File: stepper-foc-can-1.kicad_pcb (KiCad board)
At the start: 4 copper layers, 42 x 48 mm, 87 parts, among them J1 TC2030, J2 Conn_01x02, J3 Conn_01x04_Pin, J4 Conn_01x02, J5 Conn_01x02, M1 Stepper_Motor_bipolar, SW1 SW_Push, SW2 SW_Push, SW3 SW_Push, SW4 SW_Push, U1 STM32G474RBTx, U2 MX25947, U3 TPS62933, U4 TCAN3413, U5 AS5047P, U6 DRV8874, U7 INA241A3IDDF, U8 DRV8874, U9 INA241A3IDDF, Y1 Crystal_GND24

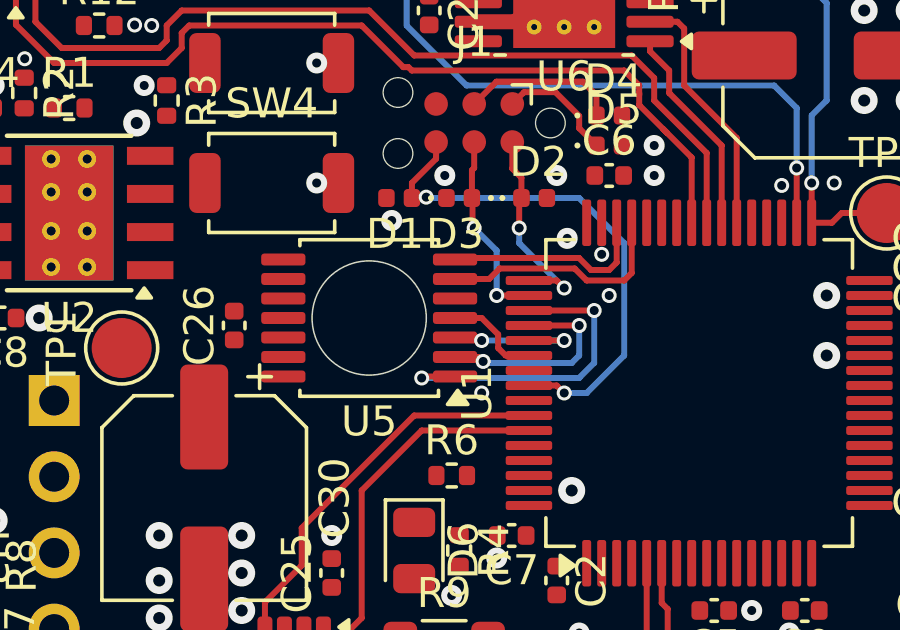
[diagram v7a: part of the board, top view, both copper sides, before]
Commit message: pcb: route encoder
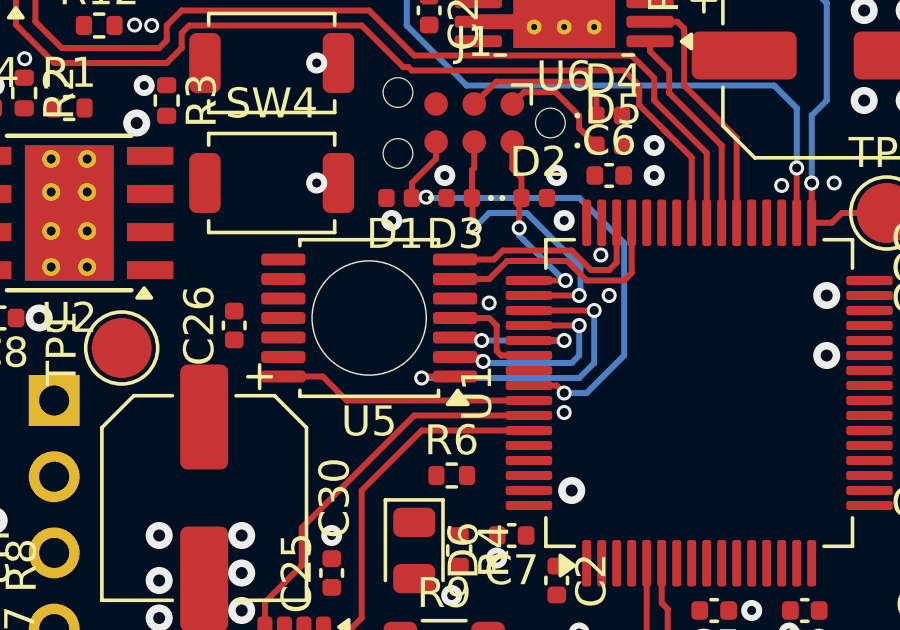
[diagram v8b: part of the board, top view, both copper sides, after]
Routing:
- net /ENC_I: track 0.00 -> 8.52 mm
- net /SWCLK: track 6.55 -> 10.1 mm
- net GND: vias 87 -> 88
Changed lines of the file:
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@@
 	)
 	(via
-		(at 150.6 78.346125)
+		(at 148 80.5)
+		(size 0.5)
+		(drill 0.3)
+		(layers "F.Cu" "B.Cu")
+		(net "GND")
+	)
+	(via
+		(at 150.5 77.75)
 		(size 0.7)
 		(drill 0.3)
@@
 	)
 	(via
-		(at 151.75 78.877587)
+		(at 151.721446 78.9)
 		(size 0.5)
 		(drill 0.3)
@@
 	)
 	(via
-		(at 147.75 83.5)
+		(at 150.5 84.150003)
 		(size 0.5)
 		(drill 0.3)
@@
 	)
 	(segment
-		(start 147.75 81)
-		(end 148.3 81.55)
+		(start 148.25 82.1)
+		(end 148.4 82.25)
 		(width 0.2)
 		(layer "F.Cu")
@@
 	(segment
 		(start 146.8625 81)
-		(end 147.75 81)
+		(end 148 81)
 		(width 0.2)
 		(layer "F.Cu")
@@
 	)
 	(segment
-		(start 148.3 81.999999)
-		(end 148.550001 82.25)
+		(start 148.25 81.25)
+		(end 148.25 82.1)
 		(width 0.2)
 		(layer "F.Cu")
@@
 	)
 	(segment
-		(start 148.550001 82.25)
+		(start 148 81)
+		(end 148.25 81.25)
+		(width 0.2)
+		(layer "F.Cu")
+		(net "/SPI_MOSI")
+	)
+	(segment
+		(start 148.4 82.25)
 		(end 149.325 82.25)
 		(width 0.2)
@@
 	)
 	(segment
-		(start 148.3 81.55)
-		(end 148.3 81.999999)
-		(width 0.2)
-		(layer "F.Cu")
-		(net "/SPI_MOSI")
+		(start 151.25 79.75)
+		(end 152.5 79.75)
+		(width 0.2)
+		(layer "F.Cu")
+		(net "/ENC_B")
+	)
+	(segment
+		(start 148.6 79.1)
+		(end 150.6 79.1)
+		(width 0.2)
+		(layer "F.Cu")
+		(net "/ENC_B")
+	)
+	(segment
+		(start 146.8625 79.7)
+		(end 148 79.7)
+		(width 0.2)
+		(layer "F.Cu")
+		(net "/ENC_B")
+	)
+	(segment
+		(start 152.5 79.75)
+		(end 152.75 79.5)
+		(width 0.2)
+		(layer "F.Cu")
+		(net "/ENC_B")
+	)
+	(segment
+		(start 148 79.7)
+		(end 148.6 79.1)
+		(width 0.2)
+		(layer "F.Cu")
+		(net "/ENC_B")
 	)
 	(segment
@@
 	)
 	(segment
-		(start 146.8625 79.7)
-		(end 148 79.7)
+		(start 150.6 79.1)
+		(end 151.25 79.75)
 		(width 0.2)
 		(layer "F.Cu")
@@
 	)
 	(segment
-		(start 150.85 79.35)
-		(end 151.25 79.75)
-		(width 0.2)
-		(layer "F.Cu")
-		(net "/ENC_B")
-	)
-	(segment
-		(start 151.25 79.75)
-		(end 152.5 79.75)
-		(width 0.2)
-		(layer "F.Cu")
-		(net "/ENC_B")
-	)
-	(segment
-		(start 148 79.7)
-		(end 148.35 79.35)
-		(width 0.2)
-		(layer "F.Cu")
-		(net "/ENC_B")
-	)
-	(segment
-		(start 148.35 79.35)
-		(end 150.85 79.35)
-		(width 0.2)
-		(layer "F.Cu")
-		(net "/ENC_B")
-	)
-	(segment
-		(start 152.5 79.75)
-		(end 152.75 79.5)
-		(width 0.2)
-		(layer "F.Cu")
-		(net "/ENC_B")
-	)
-	(segment
-		(start 150.994974 79)
-		(end 146.9125 79)
+		(start 148.455026 78.75)
+		(end 150.744974 78.75)
 		(width 0.2)
 		(layer "F.Cu")
@@
 	)
 	(segment
-		(start 152.25 77.825)
+		(start 146.8625 79.05)
+		(end 148.155026 79.05)
+		(width 0.2)
+		(layer "F.Cu")
+		(net "/ENC_A")
+	)
+	(segment
+		(start 148.155026 79.05)
+		(end 148.455026 78.75)
+		(width 0.2)
+		(layer "F.Cu")
+		(net "/ENC_A")
+	)
+	(segment
+		(start 152.25 79.15)
+		(end 152.25 77.825)
+		(width 0.2)
+		(layer "F.Cu")
+		(net "/ENC_A")
+	)
+	(segment
+		(start 150.744974 78.75)
+		(end 151.394974 79.4)
+		(width 0.2)
+		(layer "F.Cu")
+		(net "/ENC_A")
+	)
+	(segment
+		(start 151.394974 79.4)
+		(end 152 79.4)
+		(width 0.2)
+		(layer "F.Cu")
+		(net "/ENC_A")
+	)
+	(segment
+		(start 152 79.4)
 		(end 152.25 79.15)
-		(width 0.2)
-		(layer "F.Cu")
-		(net "/ENC_A")
-	)
-	(segment
-		(start 146.9125 79)
-		(end 146.8625 79.05)
-		(width 0.2)
-		(layer "F.Cu")
-		(net "/ENC_A")
-	)
-	(segment
-		(start 152.25 79.15)
-		(end 152 79.4)
-		(width 0.2)
-		(layer "F.Cu")
-		(net "/ENC_A")
-	)
-	(segment
-		(start 151.394974 79.4)
-		(end 150.994974 79)
-		(width 0.2)
-		(layer "F.Cu")
-		(net "/ENC_A")
-	)
-	(segment
-		(start 152 79.4)
-		(end 151.394974 79.4)
 		(width 0.2)
 		(layer "F.Cu")
@@
 	)
 	(segment
+		(start 143.25 83.75)
+		(end 142.45 82.95)
+		(width 0.2)
+		(layer "F.Cu")
+		(net "/ENC_I")
+	)
+	(segment
+		(start 149.325 83.75)
+		(end 143.25 83.75)
+		(width 0.2)
+		(layer "F.Cu")
+		(net "/ENC_I")
+	)
+	(segment
+		(start 142.45 82.95)
+		(end 141.1375 82.95)
+		(width 0.2)
+		(layer "F.Cu")
+		(net "/ENC_I")
+	)
+	(segment
 		(start 147.5 73.865)
 		(end 148.243699 73.121301)
@@
 	)
 	(segment
+		(start 150.542892 79.75)
+		(end 149.325 79.75)
+		(width 0.2)
+		(layer "F.Cu")
+		(net "/SWDIO")
+	)
+	(segment
 		(start 149 77.095)
 		(end 149.095 77)
@@
 	)
 	(segment
-		(start 150.25 79.75)
-		(end 150.5 80)
-		(width 0.2)
-		(layer "F.Cu")
-		(net "/SWDIO")
-	)
-	(segment
-		(start 149.325 79.75)
-		(end 150.25 79.75)
-		(width 0.2)
-		(layer "F.Cu")
-		(net "/SWDIO")
-	)
-	(segment
 		(start 149.075 76.325)
 		(end 149.075 77)
@@
 	)
 	(via
-		(at 150.5 80)
+		(at 150.542892 79.75)
 		(size 0.5)
 		(drill 0.3)
@@
 	)
 	(segment
-		(start 150.5 80)
-		(end 149 78.5)
+		(start 150.542892 79.75)
+		(end 150.5 79.75)
 		(width 0.2)
 		(layer "B.Cu")
@@
 	)
 	(segment
-		(start 149 78.5)
+		(start 149 78.25)
 		(end 149 78)
+		(width 0.2)
+		(layer "B.Cu")
+		(net "/SWDIO")
+	)
+	(segment
+		(start 150.5 79.75)
+		(end 149 78.25)
 		(width 0.2)
 		(layer "B.Cu")
@@
 	)
 	(segment
+		(start 149.325 80.25)
+		(end 151 80.25)
+		(width 0.2)
+		(layer "F.Cu")
+		(net "/SWCLK")
+	)
+	(segment
 		(start 147.5 75.135)
 		(end 147.5 76)
@@
 	)
 	(segment
-		(start 149.325 80.25)
-		(end 148.25 80.25)
-		(width 0.2)
-		(layer "F.Cu")
-		(net "/SWCLK")
-	)
-	(segment
 		(start 147.425 76.075)
 		(end 147.5 76)
@@
 	)
 	(via
-		(at 148.25 80.25)
+		(at 151 80.25)
 		(size 0.5)
 		(drill 0.3)
@@
 	)
 	(segment
-		(start 148.25 80.25)
-		(end 148.25 78.75)
+		(start 148 77.5)
+		(end 147.5 78)
 		(width 0.2)
 		(layer "B.Cu")
@@
 	)
 	(segment
-		(start 148.25 78.75)
-		(end 147.5 78)
-		(width 0.2)
-		(layer "B.Cu")
+		(start 151.042892 80.207108)
+		(end 151.042892 79.292892)
+		(width 0.2)
+		(layer "B.Cu")
+		(net "/SWCLK")
+	)
+	(segment
+		(start 149.25 77.5)
+		(end 148 77.5)
+		(width 0.2)
+		(layer "B.Cu")
+		(net "/SWCLK")
+	)
+	(segment
+		(start 151 80.25)
+		(end 151.042892 80.207108)
+		(width 0.2)
+		(layer "B.Cu")
+		(net "/SWCLK")
+	)
+	(segment
+		(start 151.042892 79.292892)
+		(end 149.25 77.5)
+		(width 0.2)
+		(layer "B.Cu")
